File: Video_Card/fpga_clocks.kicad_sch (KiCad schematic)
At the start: 7 parts, among them U7 EPF81188AQC208-3, Y1 50MHz, Y2 28.322MHz, Y3 25.175MHz

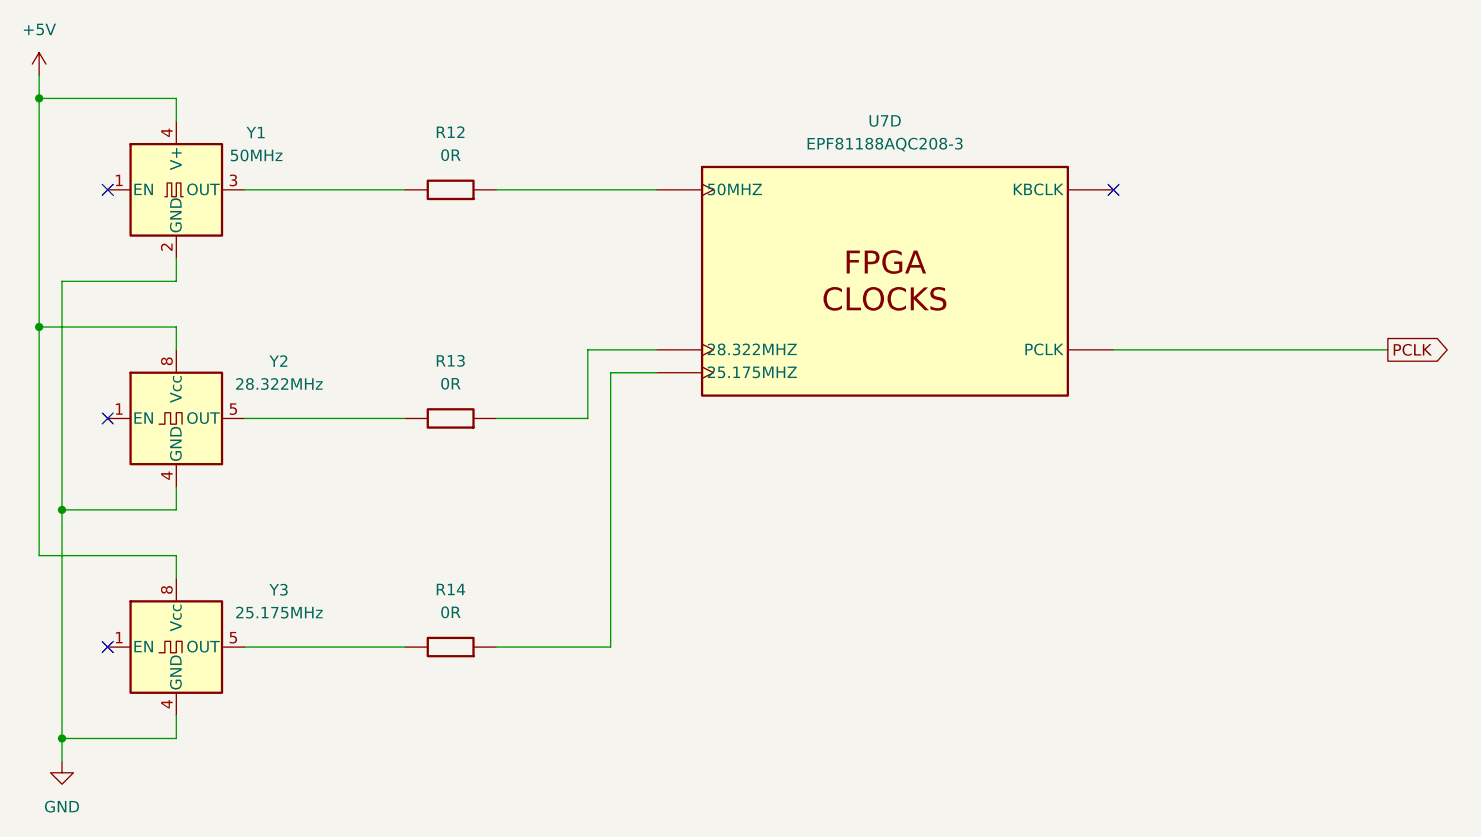
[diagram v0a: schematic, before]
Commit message: Work to date:
* added RAMDAC sheet
* tweaks to promulator circuit to disconnect MCLR, and add future reset output
* tweaks to FPGA host interface, add pin numbers and rearrange reset input to allow reset either from the system or from the promulator following configuration
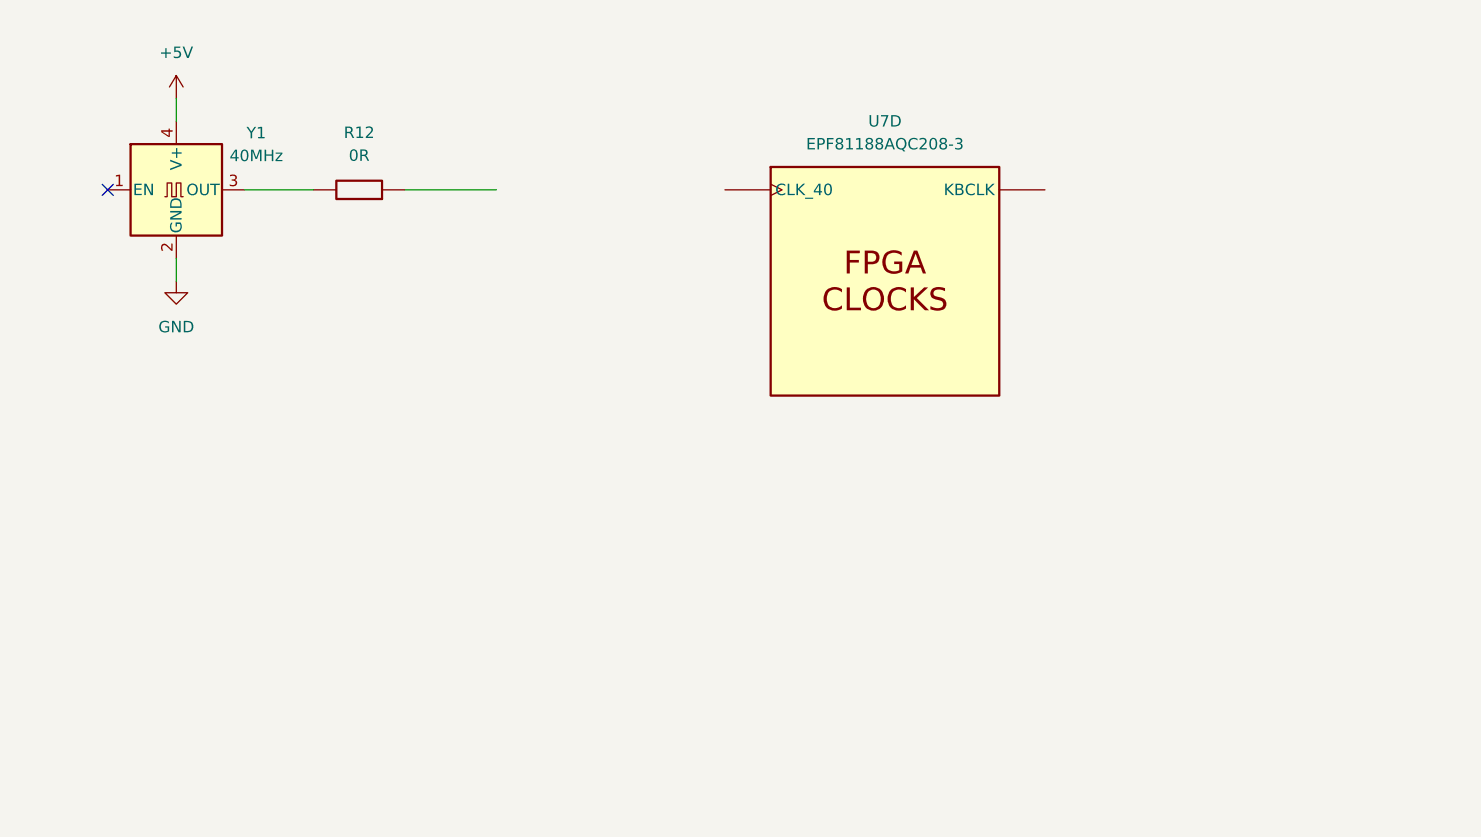
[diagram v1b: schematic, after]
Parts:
- removed R13, R14: 0R, COMET_footprints:R_SMD0805, symbol COMET_symbols:R
- removed Y2: 28.322MHz, Oscillator:Oscillator_DIP-8, symbol Oscillator:CXO_DIP8
- removed Y3: 25.175MHz, Oscillator:Oscillator_DIP-8, symbol Oscillator:CXO_DIP8
- Y1: value 50MHz -> 40MHz; footprint Oscillator:Oscillator_SMD_EuroQuartz_XO91-4Pin_7.0x5.0mm -> COMET_footprints:Oscillator_Combo_DIP-8_SMD_7x5mm
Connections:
- net at R12.2: no longer U7. (PCLK)
- removed net PCLK: U7. (PCLK)
- now unconnected: U7. (PCLK)
- no-connect marks 4 -> 1
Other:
- moved on the sheet: R12

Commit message: Work to date
So much to list ....

* Changed expansion ROM to 16 bit wide to remove some components
* Tried moving peripherals over to an 8 bit dedicated bus, but will have to revert this to reduce component count
* Fleshed out keyboard and I2C controller circuits
* Tried to fit in a font RAM, but I am 50/50 whether this will stick

And a lot more I am sure.
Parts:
- removed R12: 0R, COMET_footprints:R_SMD0805, symbol COMET_symbols:R
- removed U7: EPF81188AQC208-3, COMET_footprints:Package_PQFP-208_28x28mm_P0.5mm, symbol Video_Card:FPGA_dev
- removed Y1: 40MHz, COMET_footprints:Oscillator_Combo_DIP-8_SMD_7x5mm, symbol Oscillator:XO91
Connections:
- no-connect marks 1 -> 0
